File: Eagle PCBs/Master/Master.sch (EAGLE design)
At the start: 15 parts

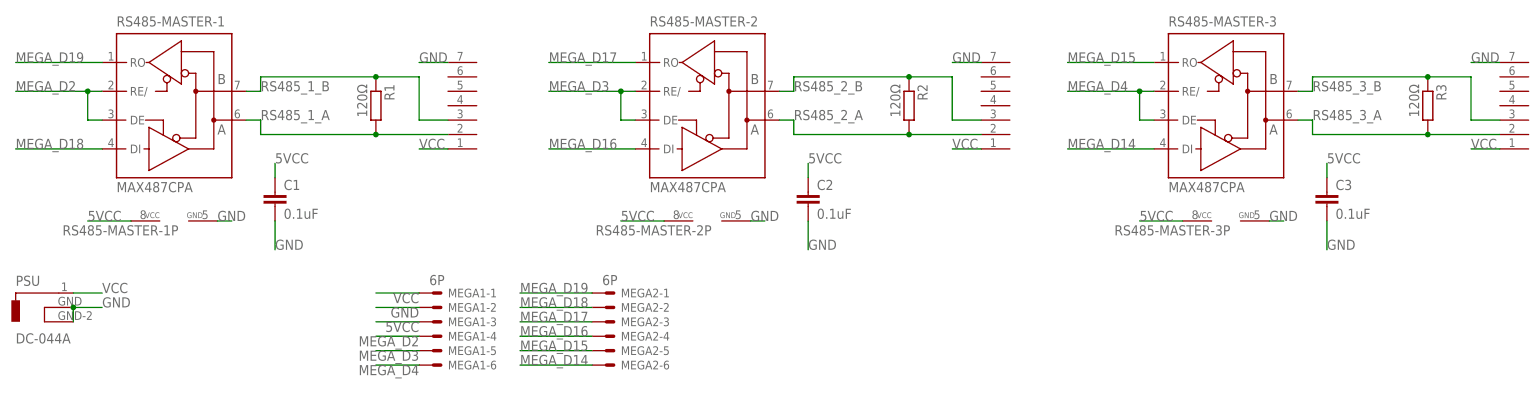
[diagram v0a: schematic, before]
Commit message: Updated GX12 footprint and finalized first revison of Master PCB
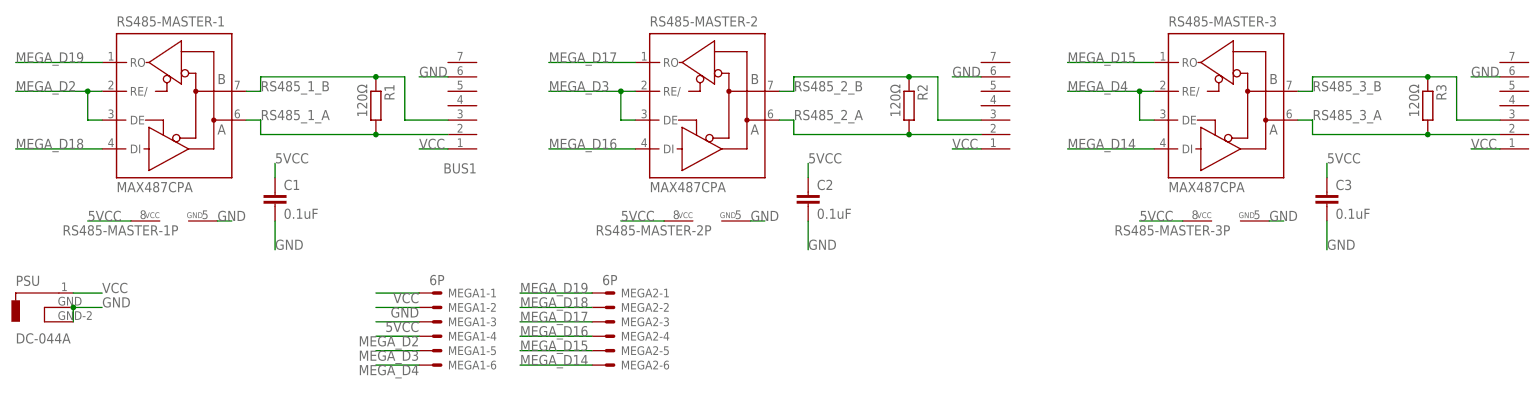
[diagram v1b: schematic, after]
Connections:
- net GND: now also BUS1.6, BUS2.6, BUS3.6; no longer BUS1.7, BUS2.7, BUS3.7
